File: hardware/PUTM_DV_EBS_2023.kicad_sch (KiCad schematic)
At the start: 0 parts

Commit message: Fixed Logic
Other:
- sheet Pressure sensor control ports: added none; removed 4, 5, 6, OUT_4, OUT_5, OUT_6
- sheet Valve Control ports: added none; removed VALVE_1_OUT, VALVE_2_OUT
- note removed: "tutaj kiedyś będzie zajeba"

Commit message: Alpha 1.0.0 Schematic
First Schematic Version for initial checkup
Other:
- sheet Pressure sensor control renamed Pressure sensor input

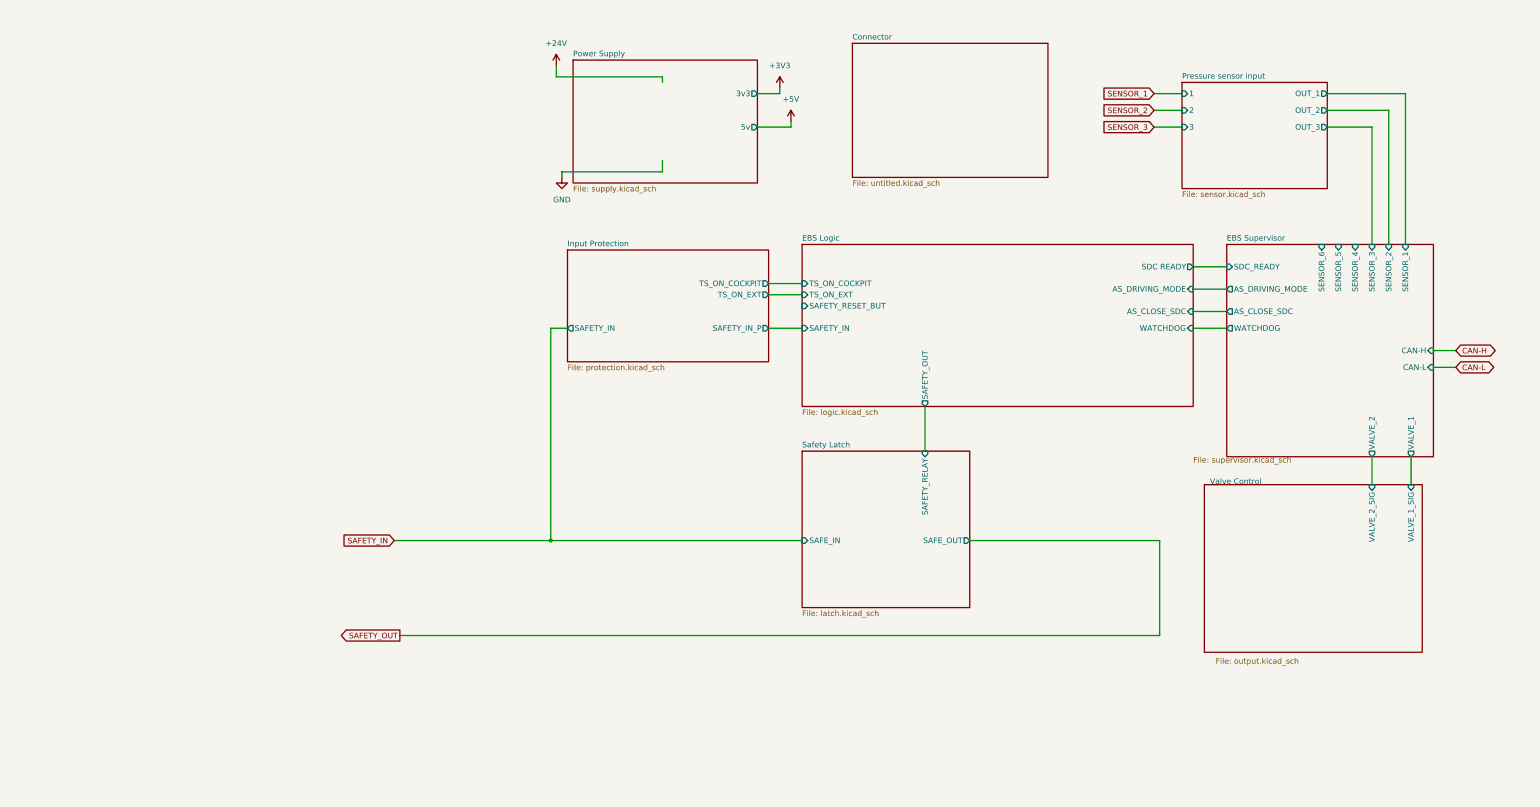
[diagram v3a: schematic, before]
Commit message: minor schematic cleanup
Fixes before second review
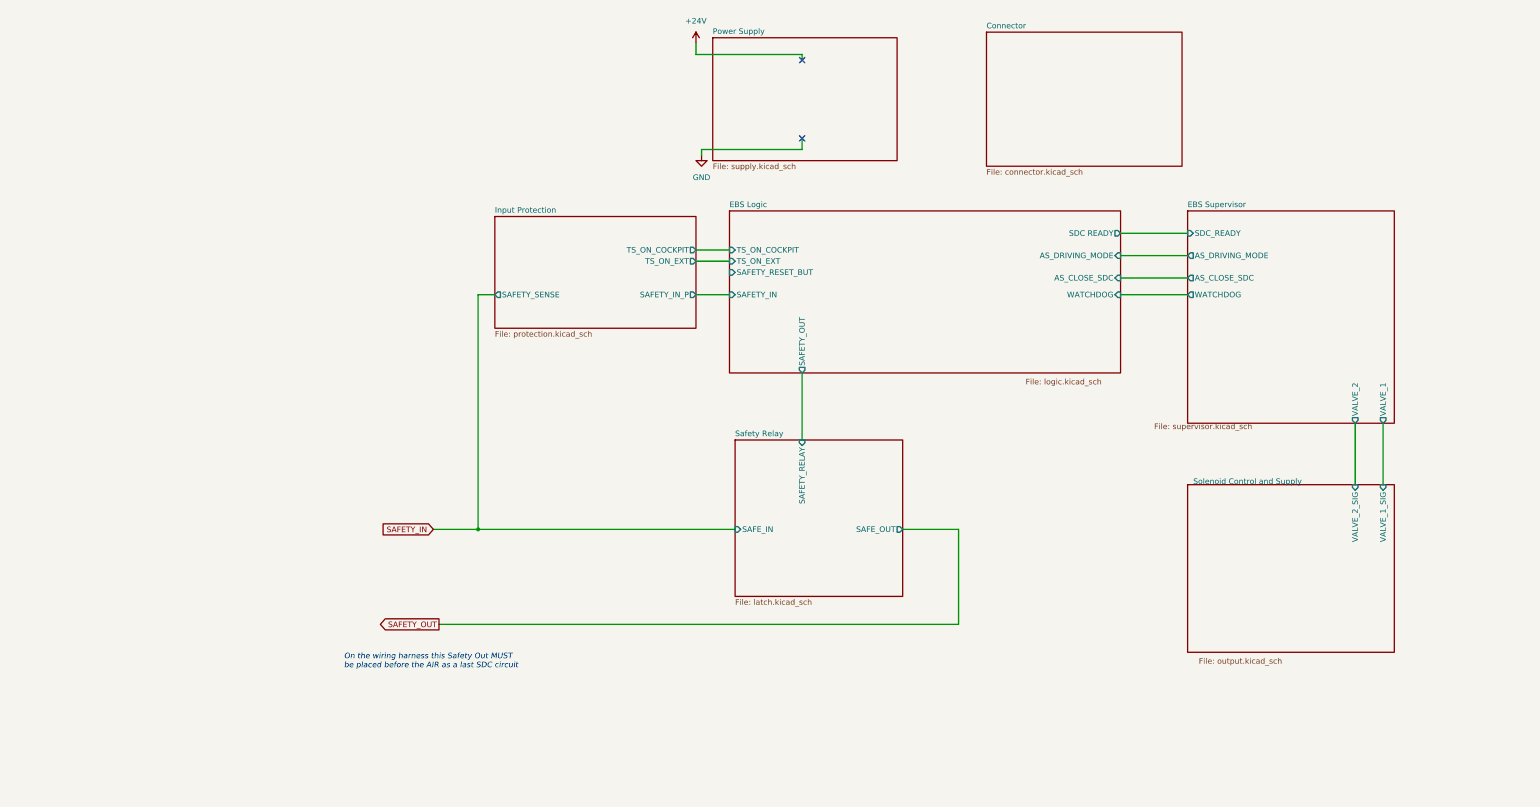
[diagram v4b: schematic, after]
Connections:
- no-connect marks 0 -> 2
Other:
- sheet Safety Latch renamed Safety Relay
- sheet Valve Control renamed Solenoid Control and Supply
- removed sheet Pressure sensor input
- sheet Connector: file untitled.kicad_sch -> connector.kicad_sch
- sheet EBS Supervisor ports: added none; removed CAN-H, CAN-L, SENSOR_1, SENSOR_2, SENSOR_3, SENSOR_4, SENSOR_5, SENSOR_6
- sheet Input Protection ports: added SAFETY_SENSE; removed SAFETY_IN
- sheet Power Supply ports: added none; removed 3v3, 5v
- note added: "On the wiring harness this Safety Out MUST be placed before the AIR as a last SDC circuit"
- company: (none) -> PUT Motorsport
- title: (none) -> General Autonomus System Brake Schematic

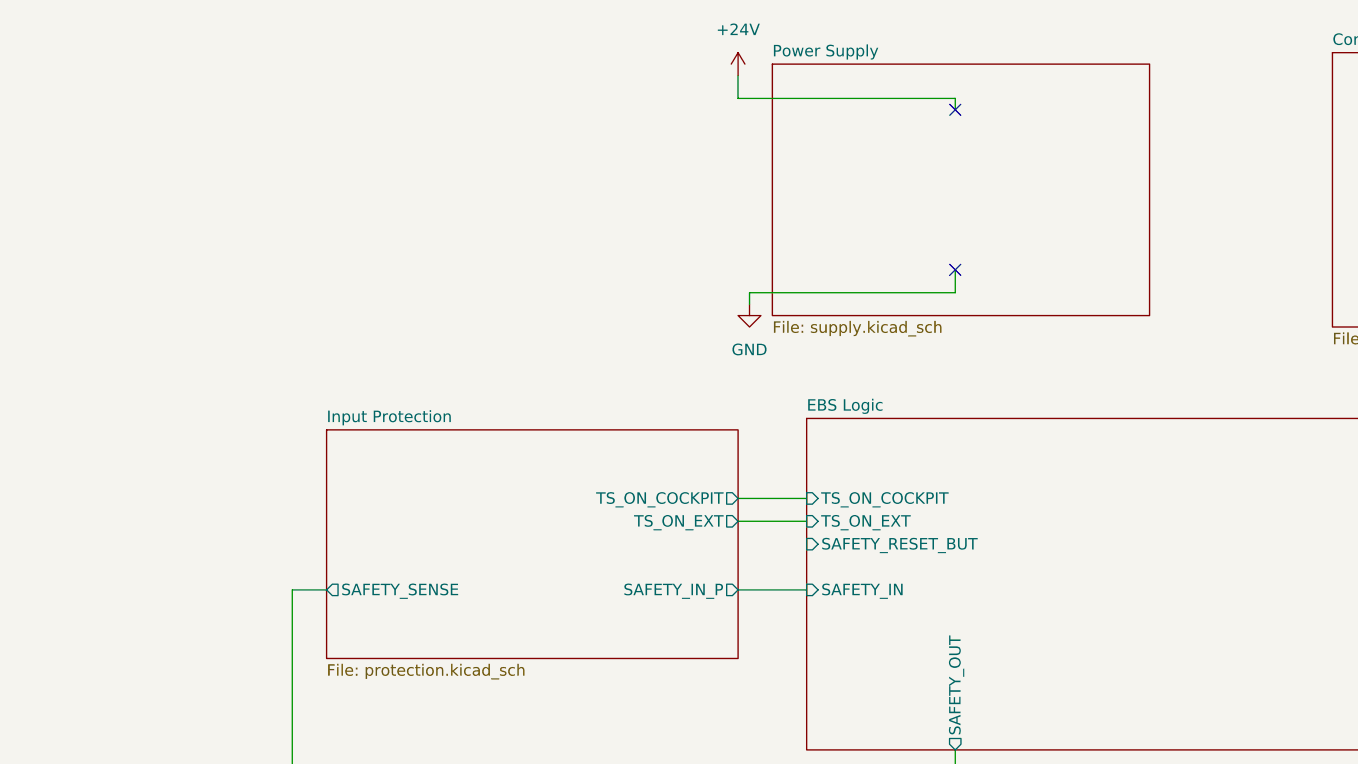
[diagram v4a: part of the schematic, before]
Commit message: Schematic ready for second review
Cleaned up, numerated, added footprints, JW notes considered
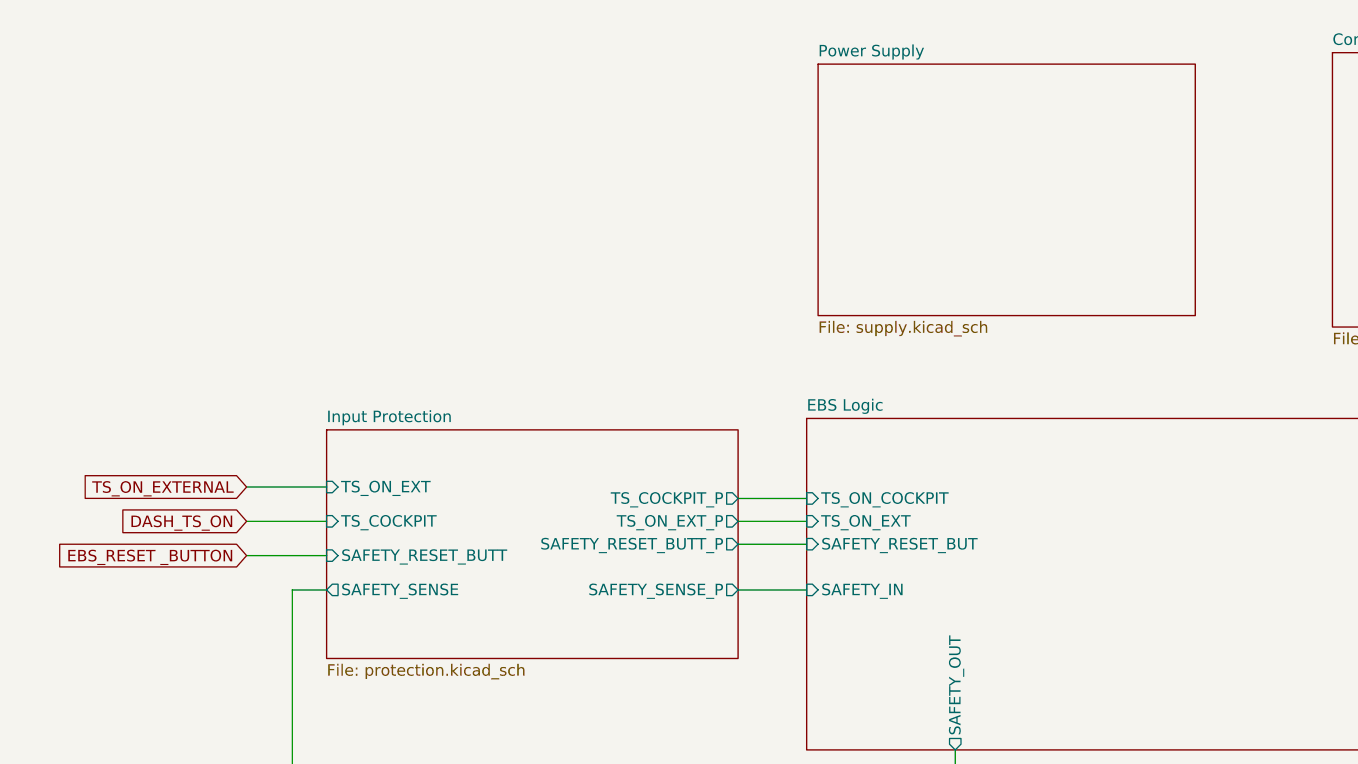
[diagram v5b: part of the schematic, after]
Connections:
- no-connect marks 2 -> 0
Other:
- sheet Input Protection ports: added SAFETY_RESET_BUTT, SAFETY_RESET_BUTT_P, SAFETY_SENSE_P, TS_COCKPIT, TS_COCKPIT_P, TS_ON_EXT_P; removed SAFETY_IN_P, TS_ON_COCKPIT

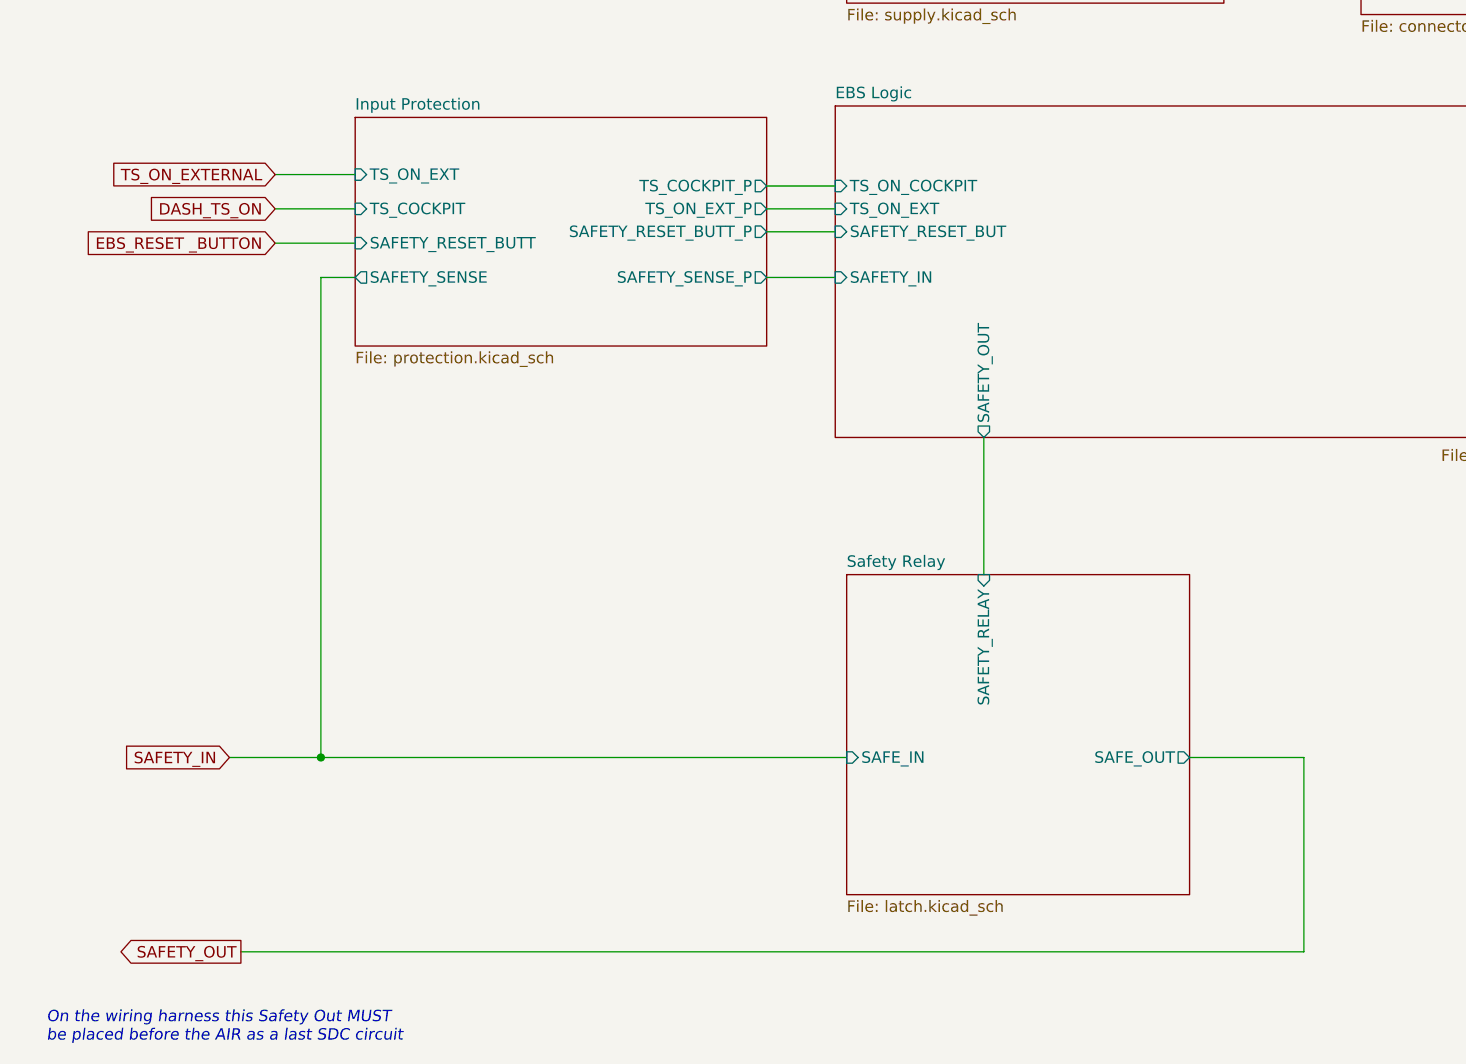
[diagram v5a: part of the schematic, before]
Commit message: 0xERC State
Schematic needs only simulation and veryfying component choice for now
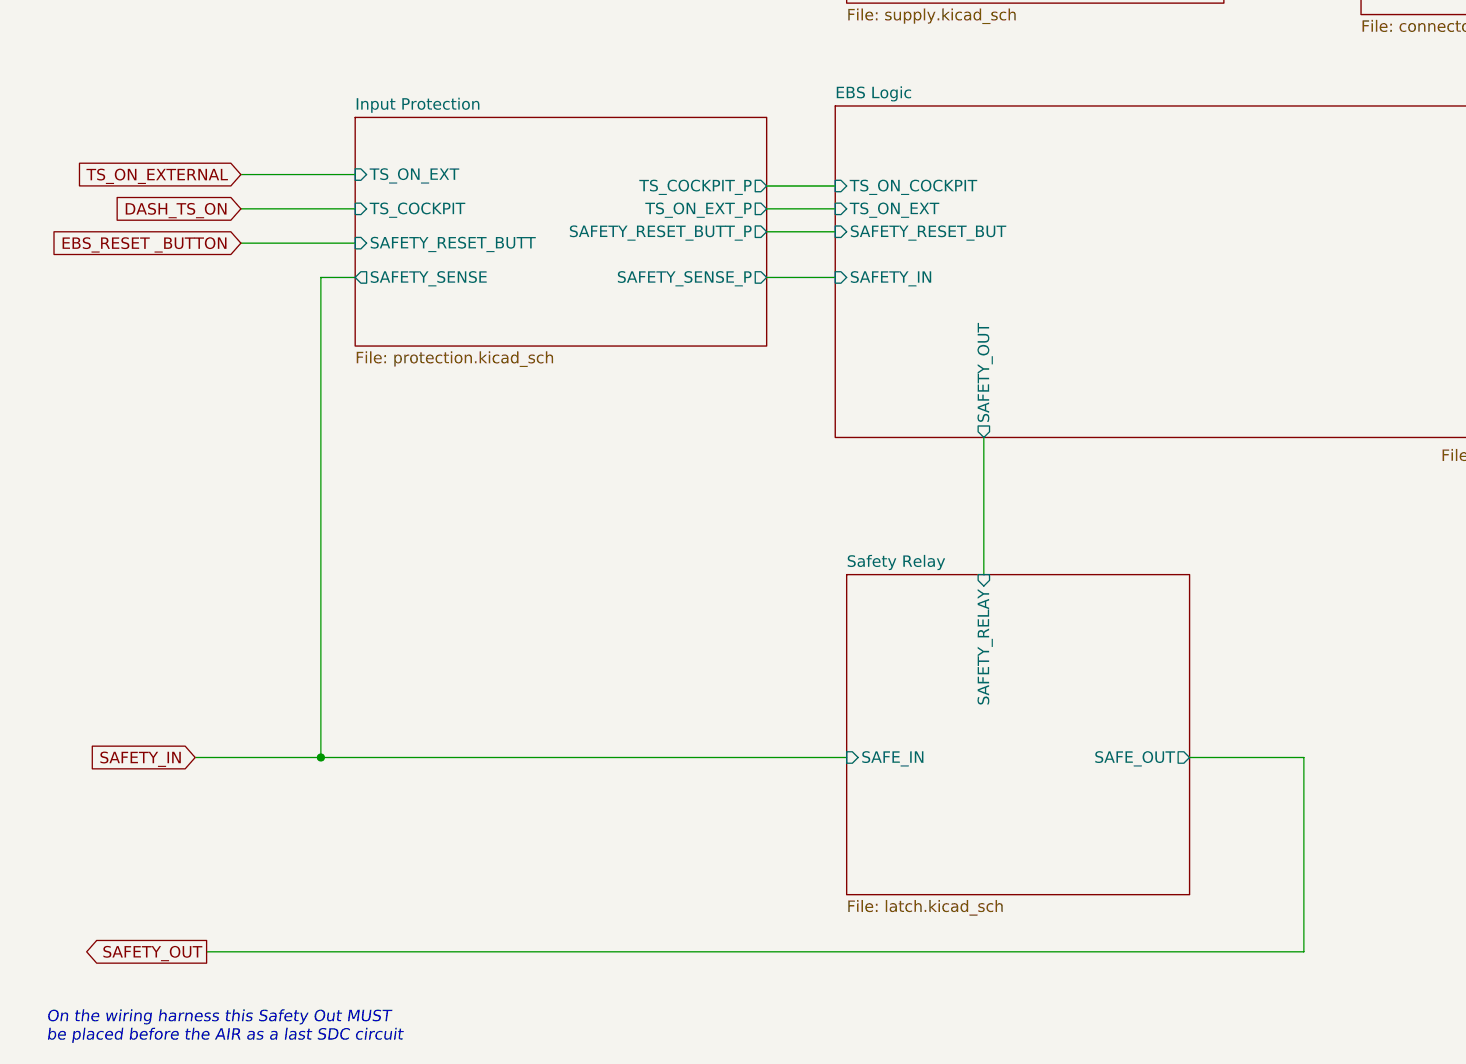
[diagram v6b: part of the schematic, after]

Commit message: Last schematic todo changes, mother slander on PCB
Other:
- added sheet Air pressure sensor control (sensors.kicad_sch)
- note added: "ADD OK ERROR WARNING LED'S"
- note added: "STM PROT 2.2K R'S"
- note added: "TO DO: 3 HIGH PRESS SENSOR INPUTS, TWO ACTUATORS, MAIN BANK"
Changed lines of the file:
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@@
     )
+  )
+  (text "ADD OK ERROR WARNING LED'S" (at 236.22 54.61 0)
+    (effects (font (size 1.27 1.27)) (justify left bottom))
+  )
+  (text "STM PROT 2.2K R'S\n" (at 214.63 54.61 0)
+    (effects (font (size 1.27 1.27)) (justify left bottom))
+  )
+  (text "TO DO: 3 HIGH PRESS SENSOR INPUTS, TWO ACTUATORS, MAIN BANK"
+    (at 214.63 50.8 0)
+    (effects (font (size 1.27 1.27)) (justify left bottom))
   )
   (text "On the wiring harness this Safety Out MUST\nbe placed before the AIR as a last SDC circuit"
@@
     (effects (font (size 1.27 1.27) italic) (justify left bottom))
   )
+  (global_label "AIR-LOW" (shape input) (at 262.89 26.67 0) (fields_autoplaced)
+    (effects (font (size 1.27 1.27)) (justify left))
+    (property "Intersheet References" "${INTERSHEET_REFS}" (id 0) (at 273.6488 26.5906 0)
+      (effects (font (size 1.27 1.27)) (justify left) hide)
+    )
+  )
   (global_label "SAFETY_IN" (shape input) (at 38.1 132.08 180) (fields_autoplaced)
     (effects (font (size 1.27 1.27)) (justify right))
@@
     )
   )
+  (global_label "AIR-LOW" (shape input) (at 262.89 21.59 0) (fields_autoplaced)
+    (effects (font (size 1.27 1.27)) (justify left))
+    (property "Intersheet References" "${INTERSHEET_REFS}" (id 0) (at 273.6488 21.5106 0)
+      (effects (font (size 1.27 1.27)) (justify left) hide)
+    )
+  )
   (global_label "EBS_RESET _BUTTON" (shape input) (at 43.18 74.93 180) (fields_autoplaced)
     (effects (font (size 1.27 1.27)) (justify right))
@@
     (property "Intersheet References" "${INTERSHEET_REFS}" (id 0) (at 24.8012 67.2306 0)
       (effects (font (size 1.27 1.27)) (justify right) hide)
+    )
+  )
+  (sheet (at 223.52 19.05) (size 36.83 25.4) (fields_autoplaced)
+    (stroke (width 0.1524) (type solid) (color 0 0 0 0))
+    (fill (color 0 0 0 0.0000))
+    (property "Sheet name" "Air pressure sensor control" (id 0) (at 223.52 18.3384 0)
+      (effects (font (size 1.27 1.27)) (justify left bottom))
+    )
+    (property "Sheet file" "sensors.kicad_sch" (id 1) (at 223.52 45.0346 0)
+      (effects (font (size 1.27 1.27)) (justify left top))
     )
   )
@@
     (path "/7da1b602-85c7-4e23-9ab2-6325d57b1abc/dae80125-d1c3-42fb-af9d-4a51941dd8ab" (page "10"))
     (path "/7da1b602-85c7-4e23-9ab2-6325d57b1abc/7e3c265d-84b6-4eba-9091-794b8ba634be" (page "11"))
+    (path "/0e6e746e-cf7c-47e8-8ed6-c681697efa7a" (page "12"))
   )
   (symbol_instances

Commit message: working simulations, assigned footprints
"nightly" relase
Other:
- sheet Air pressure sensor control ports: added EBS, MAIN, REDUNDANT, SENSOR_EBS, SENSOR_MAIN, SENSOR_REDUNDANT; removed none
- sheet EBS Supervisor ports: added AIR_EBS, AIR_MAIN, AIR_REDUNDANT; removed none
- note added: "routing, footprints left"
- note removed: "ADD OK ERROR WARNING LED'S"
- note removed: "STM PROT 2.2K R'S"
- note removed: "TO DO: 3 HIGH PRESS SENSOR INPUTS, TWO ACTUATORS, MAIN BANK"
